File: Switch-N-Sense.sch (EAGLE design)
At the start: 43 parts, among them K1 61000821121, Q1 ZXMP10A13F, Q2 FDMT80080DC, Q3 FDMT80080DC, Q4 FDMT80080DC, Q5 FDMT80080DC, U1 BQ76200

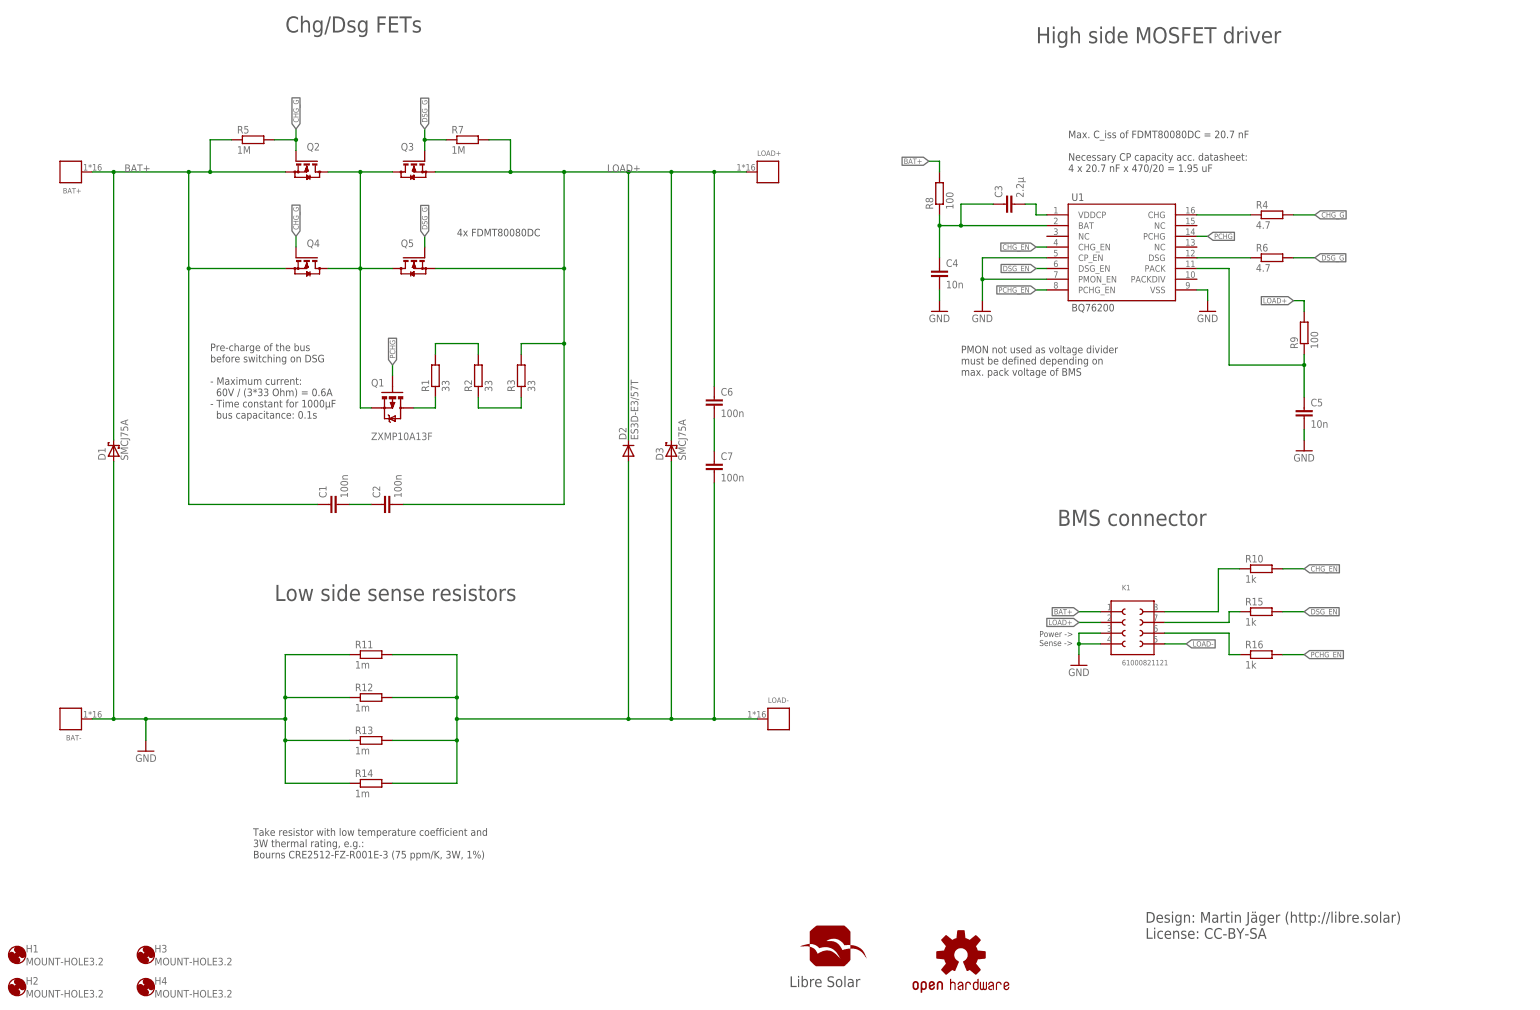
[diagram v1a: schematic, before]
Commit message: Updated board and schematic to fix issue #1
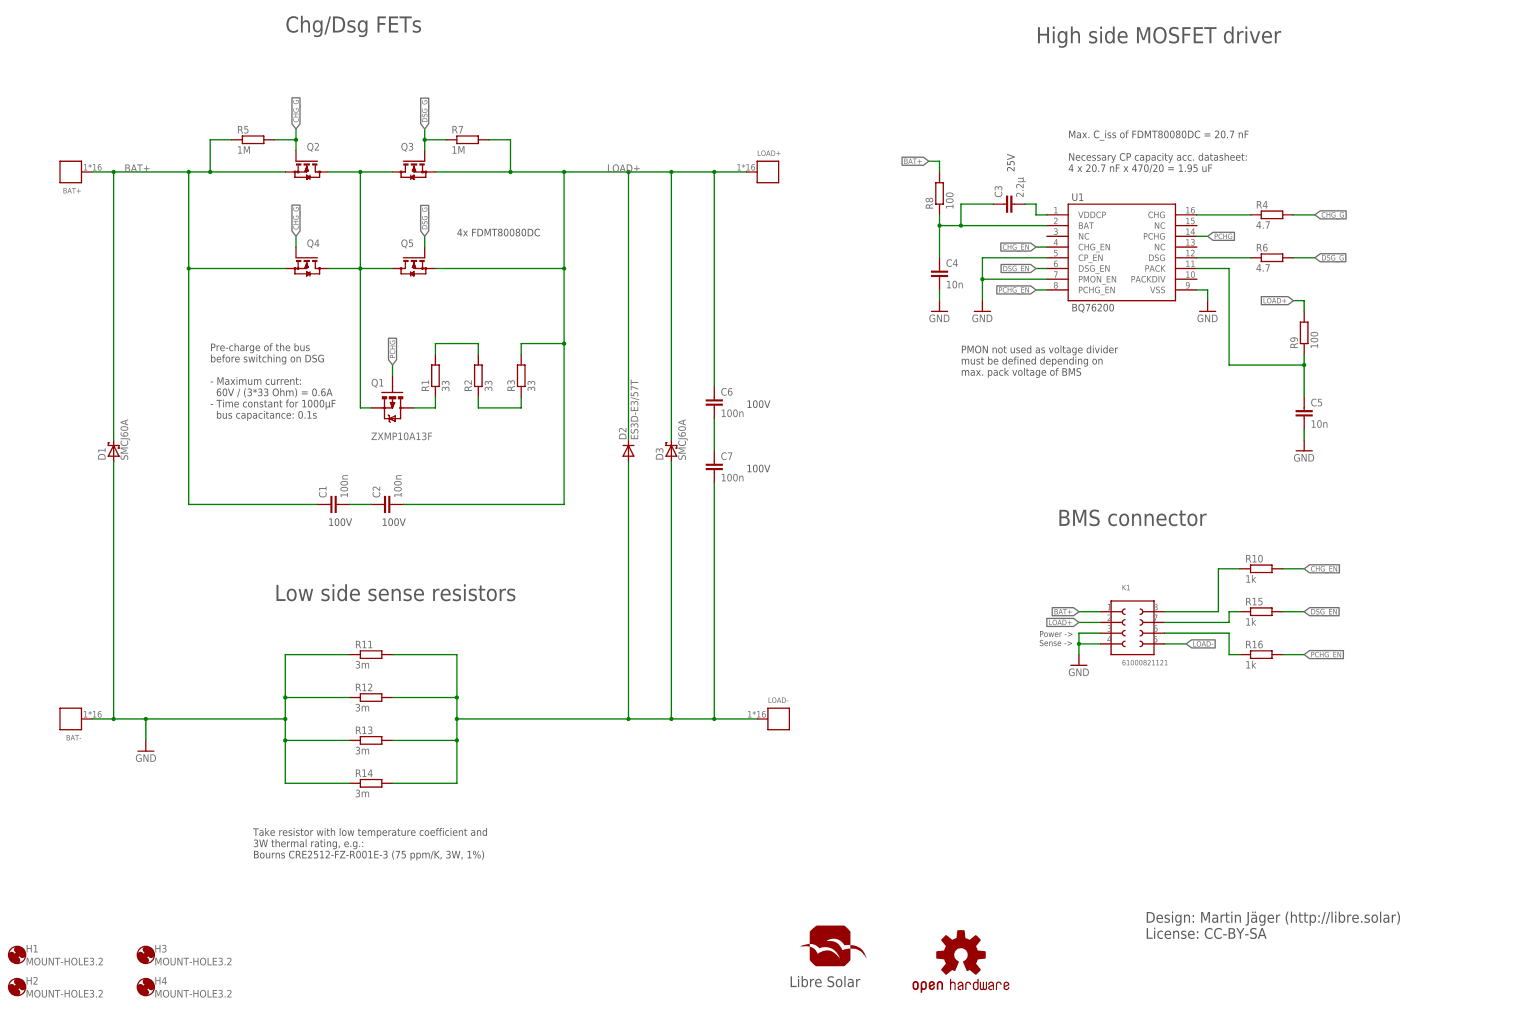
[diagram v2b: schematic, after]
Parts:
- C3: device rcl:C-EUC0603 -> rcl:C-EUC0805
- D1, D3: value SMCJ75A -> SMCJ60A
- R11, R12, R13, R14: value 1m -> 3m
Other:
- note added: "100V"
- note added: "25V"
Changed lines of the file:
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@@
 <?xml version="1.0" encoding="utf-8"?>
 <!DOCTYPE eagle SYSTEM "eagle.dtd">
-<eagle version="7.6.0">
+<eagle version="7.7.0">
 <drawing>
 <settings>
@@
 <grid distance="0.1" unitdist="inch" unit="inch" style="lines" multiple="1" display="no" altdistance="0.01" altunitdist="inch" altunit="inch"/>
 <layers>
-<layer number="1" name="Top" color="4" fill="1" visible="no" active="no"/>
-<layer number="16" name="Bottom" color="1" fill="1" visible="no" active="no"/>
-<layer number="17" name="Pads" color="2" fill="1" visible="no" active="no"/>
-<layer number="18" name="Vias" color="14" fill="1" visible="no" active="no"/>
-<layer number="19" name="Unrouted" color="6" fill="1" visible="no" active="no"/>
-<layer number="20" name="Dimension" color="15" fill="1" visible="no" active="no"/>
-<layer number="21" name="tPlace" color="7" fill="1" visible="no" active="no"/>
-<layer number="22" name="bPlace" color="7" fill="1" visible="no" active="no"/>
-<layer number="23" name="tOrigins" color="15" fill="1" visible="no" active="no"/>
-<layer number="24" name="bOrigins" color="15" fill="1" visible="no" active="no"/>
-<layer number="25" name="tNames" color="7" fill="1" visible="no" active="no"/>
-<layer number="26" name="bNames" color="7" fill="1" visible="no" active="no"/>
-<layer number="27" name="tValues" color="7" fill="1" visible="no" active="no"/>
-<layer number="28" name="bValues" color="7" fill="1" visible="no" active="no"/>
+<layer number="1" name="Top" color="4" fill="1" visible="yes" active="no"/>
+<layer number="16" name="Bottom" color="1" fill="1" visible="yes" active="no"/>
+<layer number="17" name="Pads" color="2" fill="1" visible="yes" active="no"/>
+<layer number="18" name="Vias" color="14" fill="1" visible="yes" active="no"/>
+<layer number="19" name="Unrouted" color="6" fill="1" visible="yes" active="no"/>
+<layer number="20" name="Dimension" color="15" fill="1" visible="yes" active="no"/>
+<layer number="21" name="tPlace" color="7" fill="1" visible="yes" active="no"/>
+<layer number="22" name="bPlace" color="7" fill="1" visible="yes" active="no"/>
+<layer number="23" name="tOrigins" color="15" fill="1" visible="yes" active="no"/>
+<layer number="24" name="bOrigins" color="15" fill="1" visible="yes" active="no"/>
+<layer number="25" name="tNames" color="7" fill="1" visible="yes" active="no"/>
+<layer number="26" name="bNames" color="7" fill="1" visible="yes" active="no"/>
+<layer number="27" name="tValues" color="7" fill="1" visible="yes" active="no"/>
+<layer number="28" name="bValues" color="7" fill="1" visible="yes" active="no"/>
 <layer number="29" name="tStop" color="7" fill="3" visible="no" active="no"/>
 <layer number="30" name="bStop" color="7" fill="6" visible="no" active="no"/>
@@
 <layer number="35" name="tGlue" color="7" fill="4" visible="no" active="no"/>
 <layer number="36" name="bGlue" color="7" fill="5" visible="no" active="no"/>
-<layer number="37" name="tTest" color="7" fill="1" visible="no" active="no"/>
-<layer number="38" name="bTest" color="7" fill="1" visible="no" active="no"/>
+<layer number="37" name="tTest" color="7" fill="1" visible="yes" active="no"/>
+<layer number="38" name="bTest" color="7" fill="1" visible="yes" active="no"/>
 <layer number="39" name="tKeepout" color="4" fill="11" visible="no" active="no"/>
 <layer number="40" name="bKeepout" color="1" fill="11" visible="no" active="no"/>
@@
 <layer number="44" name="Drills" color="7" fill="1" visible="no" active="no"/>
 <layer number="45" name="Holes" color="7" fill="1" visible="no" active="no"/>
-<layer number="46" name="Milling" color="3" fill="1" visible="no" active="no"/>
-<layer number="47" name="Measures" color="7" fill="1" visible="no" active="no"/>
-<layer number="48" name="Document" color="7" fill="1" visible="no" active="no"/>
-<layer number="49" name="Reference" color="7" fill="1" visible="no" active="no"/>
-<layer number="50" name="dxf" color="7" fill="1" visible="no" active="no"/>
-<layer number="51" name="tDocu" color="24" fill="1" visible="no" active="no"/>
-<layer number="52" name="bDocu" color="7" fill="1" visible="no" active="no"/>
-<layer number="53" name="tGND_GNDA" color="7" fill="1" visible="no" active="no"/>
-<layer number="54" name="bGND_GNDA" color="7" fill="1" visible="no" active="no"/>
-<layer number="56" name="wert" color="7" fill="1" visible="no" active="no"/>
-<layer number="57" name="tCAD" color="7" fill="1" visible="no" active="no"/>
-<layer number="59" name="tCarbon" color="7" fill="1" visible="no" active="no"/>
-<layer number="60" name="bCarbon" color="7" fill="1" visible="no" active="no"/>
+<layer number="46" name="Milling" color="3" fill="1" visible="yes" active="no"/>
+<layer number="47" name="Measures" color="7" fill="1" visible="yes" active="no"/>
+<layer number="48" name="Document" color="7" fill="1" visible="yes" active="no"/>
+<layer number="49" name="Reference" color="7" fill="1" visible="yes" active="no"/>
+<layer number="50" name="dxf" color="7" fill="1" visible="yes" active="no"/>
+<layer number="51" name="tDocu" color="24" fill="1" visible="yes" active="no"/>
+<layer number="52" name="bDocu" color="7" fill="1" visible="yes" active="no"/>
+<layer number="53" name="tGND_GNDA" color="7" fill="1" visible="yes" active="no"/>
+<layer number="54" name="bGND_GNDA" color="7" fill="1" visible="yes" active="no"/>
+<layer number="56" name="wert" color="7" fill="1" visible="yes" active="no"/>
+<layer number="57" name="tCAD" color="7" fill="1" visible="yes" active="no"/>
+<layer number="59" name="tCarbon" color="7" fill="1" visible="yes" active="no"/>
+<layer number="60" name="bCarbon" color="7" fill="1" visible="yes" active="no"/>
 <layer number="90" name="Modules" color="5" fill="1" visible="yes" active="yes"/>
 <layer number="91" name="Nets" color="2" fill="1" visible="yes" active="yes"/>
@@
 <attribute name="OC_FARNELL" value="8819980"/>
 </part>
-<part name="C3" library="rcl" deviceset="C-EU" device="C0603" value="2.2µ">
+<part name="C3" library="rcl" deviceset="C-EU" device="C0805" value="2.2µ">
 <attribute name="MF" value="WALSIN"/>
 <attribute name="MPN" value="0603B104K500CT"/>
@@
 <part name="LOAD-" library="Wuerth_Elektronik_Power_Elements_rev15c" deviceset="WP-BUCF" device="_G"/>
 <part name="GND3" library="supply1" deviceset="GND" device=""/>
-<part name="R11" library="rcl" deviceset="R-EU_" device="R2512" value="1m">
-<attribute name="MF" value=""/>
-<attribute name="MPN" value=""/>
-<attribute name="OC_FARNELL" value="unknown"/>
-</part>
-<part name="R12" library="rcl" deviceset="R-EU_" device="R2512" value="1m">
-<attribute name="MF" value=""/>
-<attribute name="MPN" value=""/>
-<attribute name="OC_FARNELL" value="unknown"/>
-</part>
-<part name="R13" library="rcl" deviceset="R-EU_" device="R2512" value="1m">
-<attribute name="MF" value=""/>
-<attribute name="MPN" value=""/>
-<attribute name="OC_FARNELL" value="unknown"/>
-</part>
-<part name="R14" library="rcl" deviceset="R-EU_" device="R2512" value="1m">
-<attribute name="MF" value=""/>
-<attribute name="MPN" value=""/>
-<attribute name="OC_FARNELL" value="unknown"/>
-</part>
-<part name="D1" library="diode" deviceset="SCHOTTKY-DIODE" device="SMC" value="SMCJ75A">
+<part name="R11" library="rcl" deviceset="R-EU_" device="R2512" value="3m">
+<attribute name="MF" value=""/>
+<attribute name="MPN" value=""/>
+<attribute name="OC_FARNELL" value="unknown"/>
+</part>
+<part name="R12" library="rcl" deviceset="R-EU_" device="R2512" value="3m">
+<attribute name="MF" value=""/>
+<attribute name="MPN" value=""/>
+<attribute name="OC_FARNELL" value="unknown"/>
+</part>
+<part name="R13" library="rcl" deviceset="R-EU_" device="R2512" value="3m">
+<attribute name="MF" value=""/>
+<attribute name="MPN" value=""/>
+<attribute name="OC_FARNELL" value="unknown"/>
+</part>
+<part name="R14" library="rcl" deviceset="R-EU_" device="R2512" value="3m">
+<attribute name="MF" value=""/>
+<attribute name="MPN" value=""/>
+<attribute name="OC_FARNELL" value="unknown"/>
+</part>
+<part name="D1" library="diode" deviceset="SCHOTTKY-DIODE" device="SMC" value="SMCJ60A">
 <attribute name="MF" value="FAIRCHILD SEMICONDUCTOR"/>
 <attribute name="MPN" value="SMCJ75A"/>
@@
 <attribute name="OC_FARNELL" value="1021753"/>
 </part>
-<part name="D3" library="diode" deviceset="SCHOTTKY-DIODE" device="SMC" value="SMCJ75A">
+<part name="D3" library="diode" deviceset="SCHOTTKY-DIODE" device="SMC" value="SMCJ60A">
 <attribute name="MF" value="FAIRCHILD SEMICONDUCTOR"/>
 <attribute name="MPN" value="SMCJ75A"/>
@@
 must be defined depending on
 max. pack voltage of BMS</text>
+<text x="195.58" y="152.4" size="1.778" layer="97">100V</text>
+<text x="195.58" y="137.16" size="1.778" layer="97">100V</text>
+<text x="109.22" y="124.46" size="1.778" layer="97">100V</text>
+<text x="96.52" y="124.46" size="1.778" layer="97">100V</text>
+<text x="259.08" y="208.28" size="1.778" layer="97" rot="R90">25V</text>
 </plain>
 <instances>
